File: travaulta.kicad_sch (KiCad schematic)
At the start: 31 parts, among them J2 JST, Q1 2N7002, SW38 SW_MEC_5G, U1 STM32F411CCUx, U2 XC6206PxxxMR, Y1 16 MHz

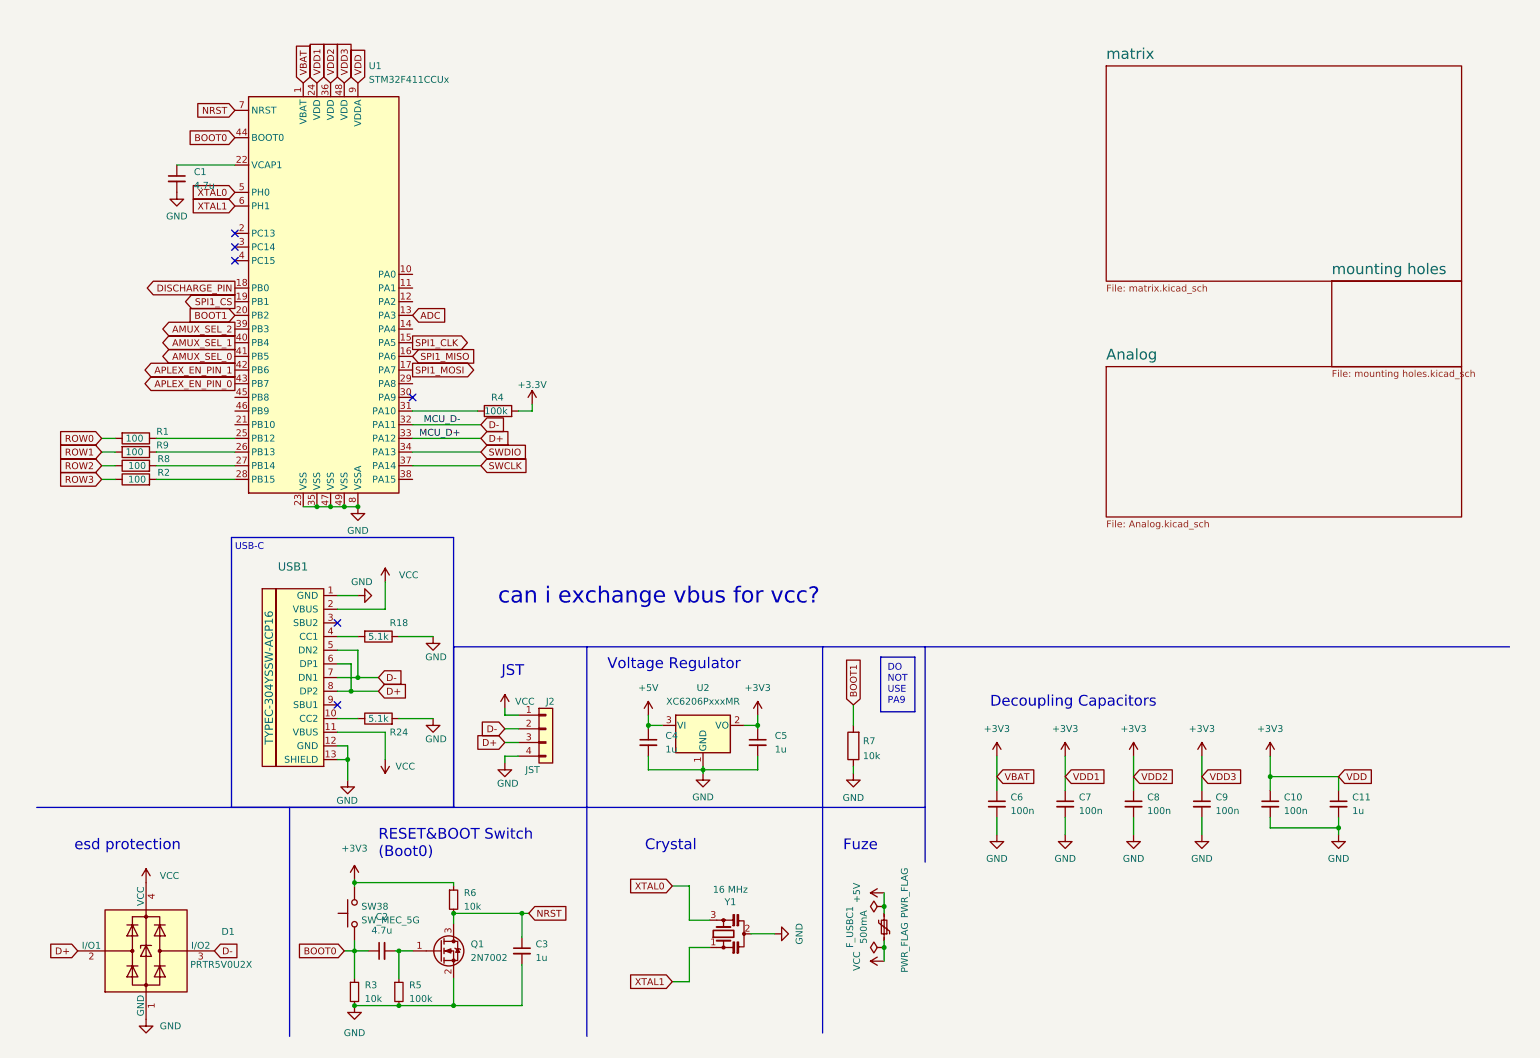
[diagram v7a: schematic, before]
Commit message: clean up folders, edit silkscreen
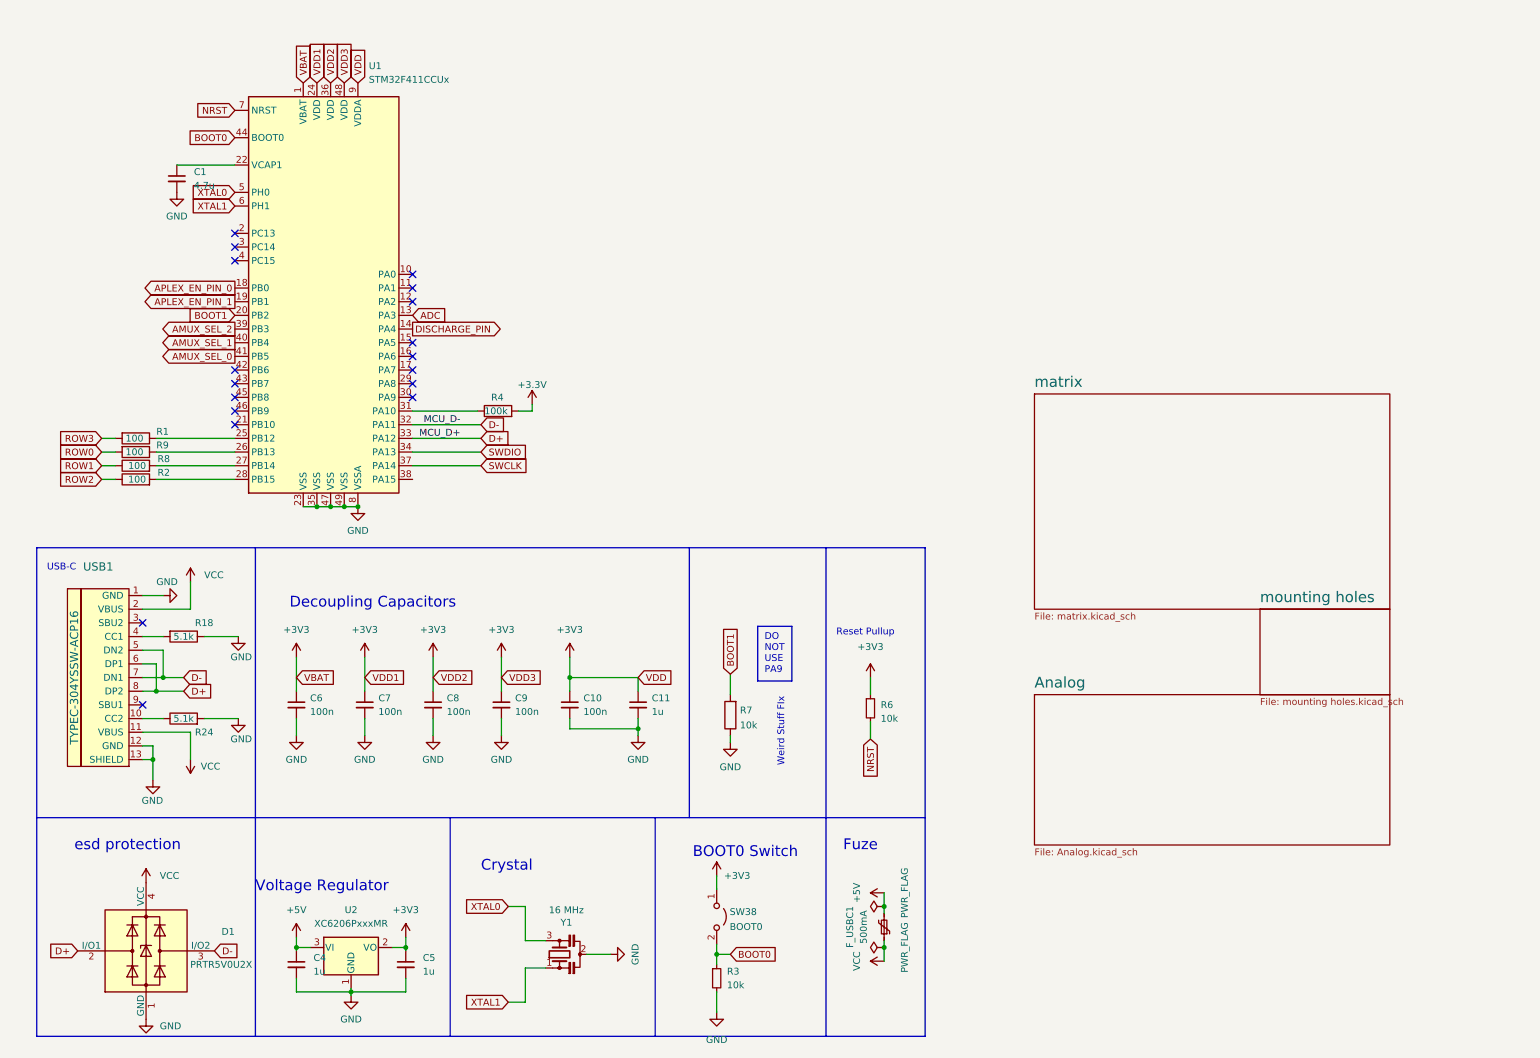
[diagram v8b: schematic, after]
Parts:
- removed C2: 4.7u, Capacitor_SMD:C_0402_1005Metric, symbol Device:C_Small
- removed C3: 1u, Capacitor_SMD:C_0402_1005Metric, symbol Device:C_Small
- removed J2: JST, cipulot_parts:JST-SR-4, symbol Connector_Generic:Conn_01x04
- removed Q1: 2N7002, Package_TO_SOT_SMD:SOT-23, symbol Transistor_FET:2N7002
- removed R5: 100k, Resistor_SMD:R_0402_1005Metric, symbol Device:R_Small
- removed SW38: SW_MEC_5G, cipulot_parts:SW_SPST_TL3342, symbol Switch:SW_MEC_5G
- added SW38: BOOT0, Connector_PinHeader_2.54mm:PinHeader_1x02_P2.54mm_Vertical, symbol Jumper:Jumper_2_Open
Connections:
- net SPI1_CS is gone; now on net APLEX_EN_PIN_1: U1.19 (PB1)
- net +3V3: now also SW38.1 (A)
- net APLEX_EN_PIN_0: now also U1.18 (PB0); no longer U1.43 (PB7)
- net APLEX_EN_PIN_1: no longer U1.42 (PB6)
- net BOOT0: now also SW38.2 (B)
- net DISCHARGE_PIN: now also U1.14 (PA4); no longer U1.18 (PB0)
- net ROW0: now also R9.2; no longer R1.2
- net ROW1: now also R8.1; no longer R9.2
- net ROW2: now also R2.1; no longer R8.1
- net ROW3: now also R1.2; no longer R2.1
- net SPI1_CLK: no longer names the net of U1.15 (PA5)
- net SPI1_MISO: no longer names the net of U1.16 (PA6)
- net SPI1_MOSI: no longer names the net of U1.17 (PA7)
- no-connect marks 6 -> 18
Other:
- note added: "BOOT0 Switch"
- note added: "Reset Pullup"
- note added: "Weird Stuff FIx"
- note removed: "JST"
- note removed: "RESET&BOOT Switch (Boot0)"
- note removed: "can i exchange vbus for vcc?"
- moved on the sheet: C10, C11, C4, C5, C6, C7, C8, C9, R18, R24, R3, R6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
